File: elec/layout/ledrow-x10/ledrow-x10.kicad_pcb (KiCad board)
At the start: 2 copper layers, 20 parts, among them U1 ?, U10 ?, U2 ?, U3 ?, U4 ?, U5 ?, U6 ?, U7 ?, U8 ?, U9 ?

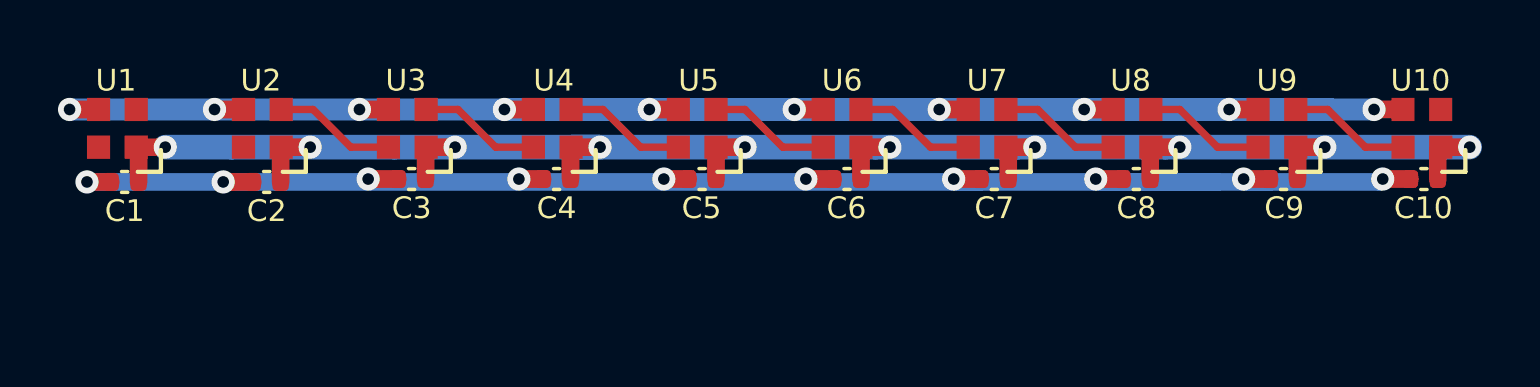
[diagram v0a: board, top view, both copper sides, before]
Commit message: removed usb-uart
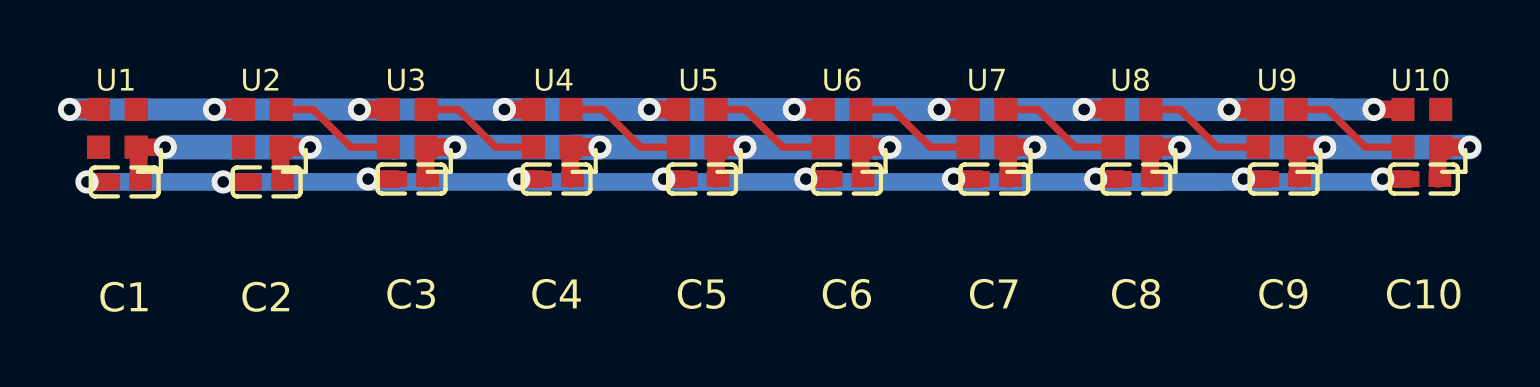
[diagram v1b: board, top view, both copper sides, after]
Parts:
- C1, C10, C2, C3, C4, C5, C6, C7, C8, C9: value 16V 100nF X7R ±10% 0402 Multilayer Ceramic Capacitors MLCC - SMD/SMT ROHS -> 100nF ±10% 16V X7R; footprint lib:C0402 -> atopile:C0402-b3ef17
- U1, U10, U2, U3, U4, U5, U6, U7, U8, U9: value ? -> (none)
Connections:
- net din renamed DIN
- net dout renamed DOUT
- net led1.ic-vcc renamed io-4
- net led3.ic-vcc renamed io-1
- net led4.ic-vcc renamed vcc-1
- net led5.ic-vcc renamed io-3
- net led6.ic-vcc renamed io-2
- net led7.ic-vcc renamed vcc-3
- net led8.ic-vcc renamed io
- net led9.ic-vcc renamed vcc-2
- C1 pad 1: vcc -> hv
- C10 pad 1: vcc -> hv
- C2 pad 1: vcc -> hv
- C3 pad 1: vcc -> hv
- C4 pad 1: vcc -> hv
- C5 pad 1: vcc -> hv
- C6 pad 1: vcc -> hv
- C7 pad 1: vcc -> hv
- C8 pad 1: vcc -> hv
- C9 pad 1: vcc -> hv
- U1 pad 1: vcc -> hv
- U10 pad 1: vcc -> hv
- U2 pad 1: vcc -> hv
- U2 pad 2: led2.ic-vcc -> vcc
- U3 pad 1: vcc -> hv
- U3 pad 4: led2.ic-vcc -> vcc
- U4 pad 1: vcc -> hv
- U5 pad 1: vcc -> hv
- U6 pad 1: vcc -> hv
- U7 pad 1: vcc -> hv
- U8 pad 1: vcc -> hv
- U9 pad 1: vcc -> hv
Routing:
- net hv: track 0.00 -> 75.5 mm, vias 0 -> 10
- net vcc: track 75.5 -> 4.24 mm, vias 10 -> 0
- net led2.ic-vcc: track 4.24 -> 0.00 mm
